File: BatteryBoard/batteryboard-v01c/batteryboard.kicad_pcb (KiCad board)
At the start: 2 copper layers, 95.9 x 90.2 mm, 27 parts, among them J1 KEYSTONE-1042, J12 Screw_Terminal_01x02, J2 KEYSTONE-1042, J3 KEYSTONE-1042, J4 KEYSTONE-1042, J5 KEYSTONE-1042, J6 KEYSTONE-1042, J7 5023520400, J8 Screw_Terminal_01x02, Q1 IRF7458, Q2 IRF7458, U1 R5460N233AF

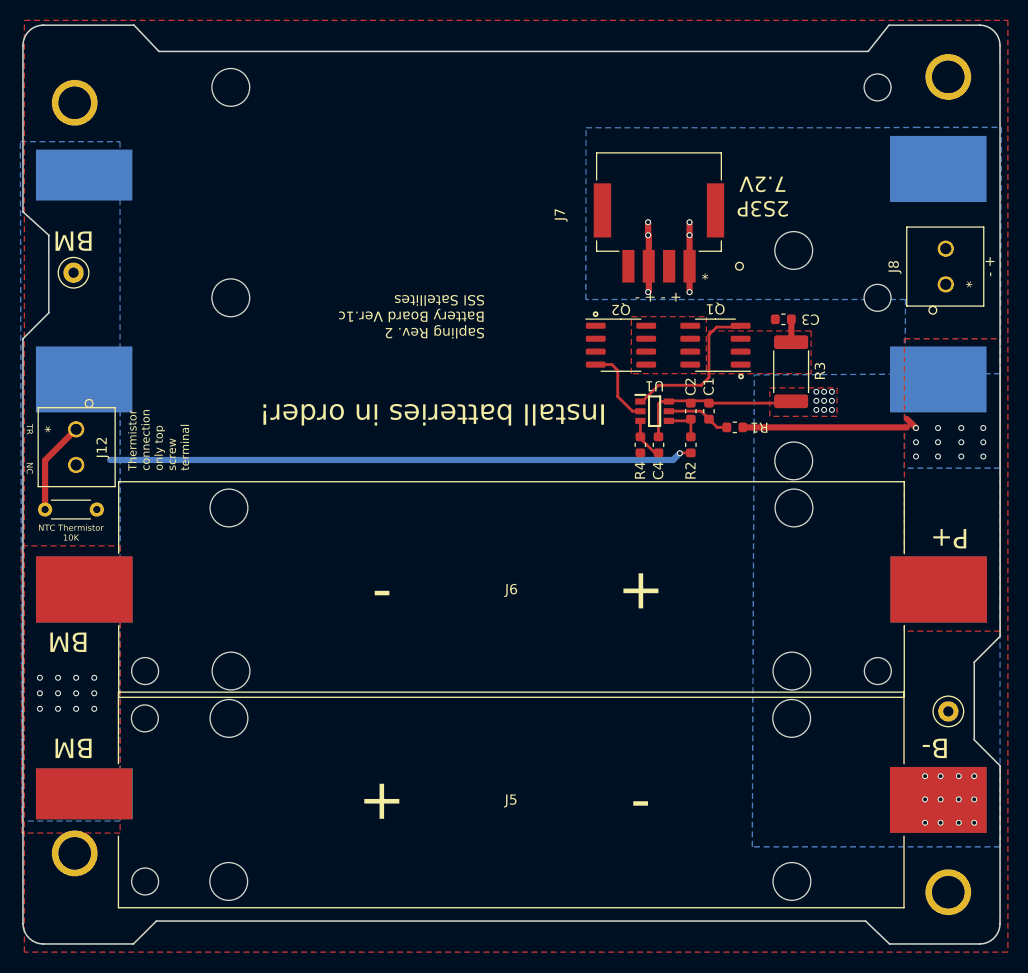
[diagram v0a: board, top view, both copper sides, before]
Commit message: Battery board and side panels ready for CAD check and review, pycubed not finished yet
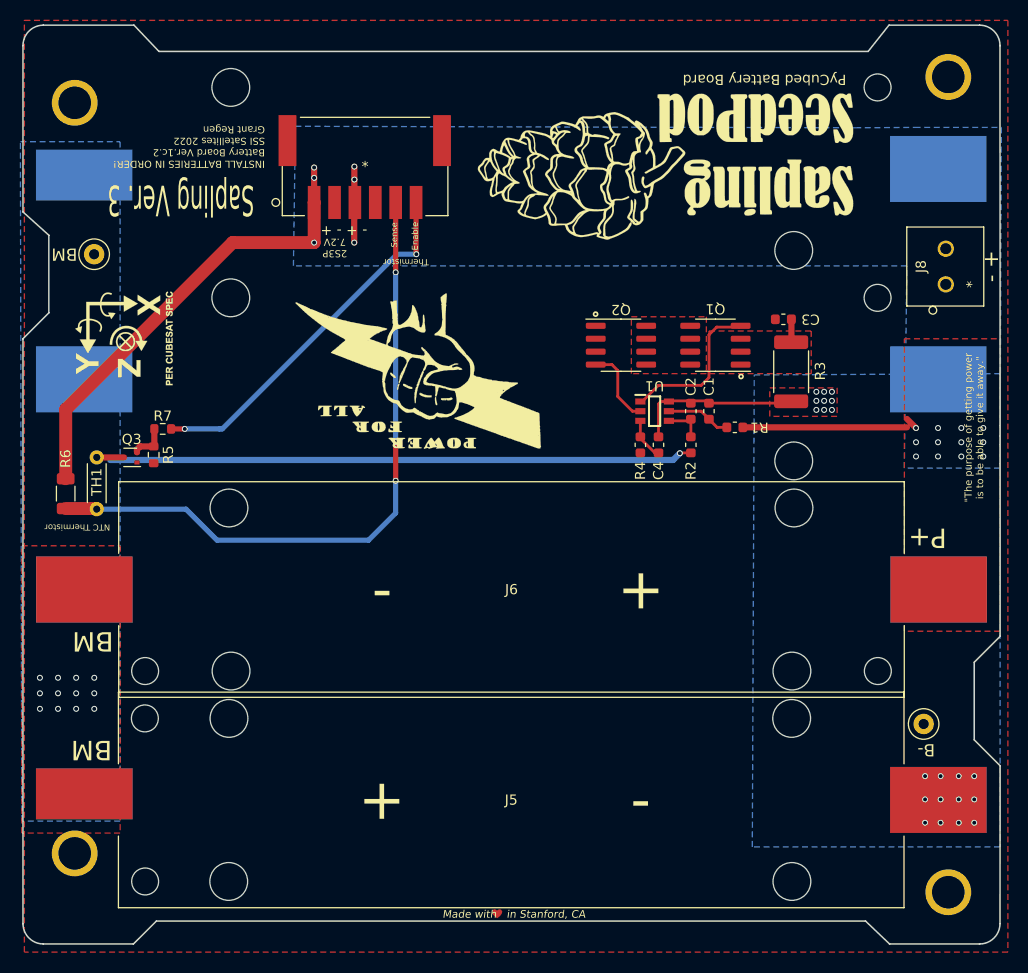
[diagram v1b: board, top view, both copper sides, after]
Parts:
- removed J12: Screw_Terminal_01x02, batteryboard:pheonix_2pos_screwterminal
- added Made with   in Stanford, CA: Val**, batteryboard:SSI_KiCad_Heart, F.Cu at (99.7, 141.1)
- added Q3: MMBT2222AT, Package_TO_SOT_SMD:SOT-523, F.Cu at (63.7, 96.2)
- added R5: 100k, Resistor_SMD:R_0603_1608Metric, F.Cu at (66.0, 96.0)
- added R6: 200k, Resistor_SMD:R_1206_3216Metric, F.Cu at (57.4, 99.8)
- added R7: 200k, Resistor_SMD:R_0603_1608Metric, F.Cu at (66.9, 93.4)
- added Ref**: Val**, batteryboard:XYZ_cubesat-bot, B.Cu at (63.1, 84.5)
- added Ref**: Val**, batteryboard:PowerLogo, F.Cu at (92.4, 87.7)
- added Ref**: Val**, batteryboard:SeedPodLogo, F.Cu at (115.9, 67.0)
- J7: value 5023520400 -> 5023520601; footprint batteryboard:duraclik_4pos -> batteryboard:5023520600
- TH1: value Thermistor -> TTDO-10KC8-3-1%
- moved J7 33.3 mm to (86.8, 67.7)
- moved TH1 5.07 mm to (60.4, 101.3), turned to 90 degrees
- moved TP1 2.72 mm to (141.6, 122.4)
- moved TP2 2.72 mm to (60.2, 76.3)
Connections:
- J7 pad 5: (no net) -> PyCubed_AIN5
- J7 pad 6: (no net) -> DigitalPinTBD
- TH1 pad 1: BAT_THERM -> PyCubed_AIN5
- TH1 pad 2: PACK- -> Net-(Q3-Pad3)
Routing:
- net PyCubed_AIN5: track 0.00 -> 65.3 mm, vias 0 -> 3
- net PACK+: track 31.1 -> 70.2 mm
- net DigitalPinTBD: track 0.00 -> 36.3 mm, vias 0 -> 2
- net BAT_THERM: track 9.14 -> 0.00 mm
- net Net-(Q3-Pad2): track 0.00 -> 3.78 mm
- net Net-(Q3-Pad3): track 0.00 -> 2.66 mm
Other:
- board text added: ""The purpose of getting power is to be able to give it away.""
- board text added: "Enable"
- board text added: "INSTALL BATTERIES IN ORDER! Battery Board Ver.1c.2 SSI Satellites 2022 Grant Regen"
- board text added: "NTC Thermistor"
- board text added: "PyCubed Battery Board"
- board text added: "REGEN"
- board text added: "Sapling Ver. 3"
- board text added: "Sense"
- board text added: "Thermistor"
- board text removed: "Install batteries in order!"
- board text removed: "NC"
- board text removed: "NTC Thermistor 10K"
- board text removed: "Sapling Rev. 2 Battery Board Ver.1c SSI Satellites"
- board text removed: "TR"
- board text removed: "Thermistor connection only top screw terminal"

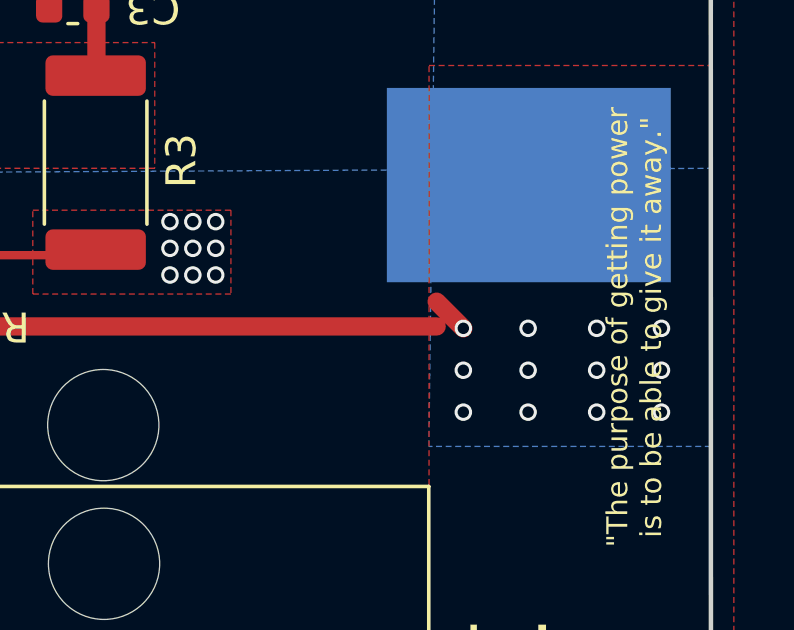
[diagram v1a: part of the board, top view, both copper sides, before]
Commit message: radio and gps moved to make space for limit switches
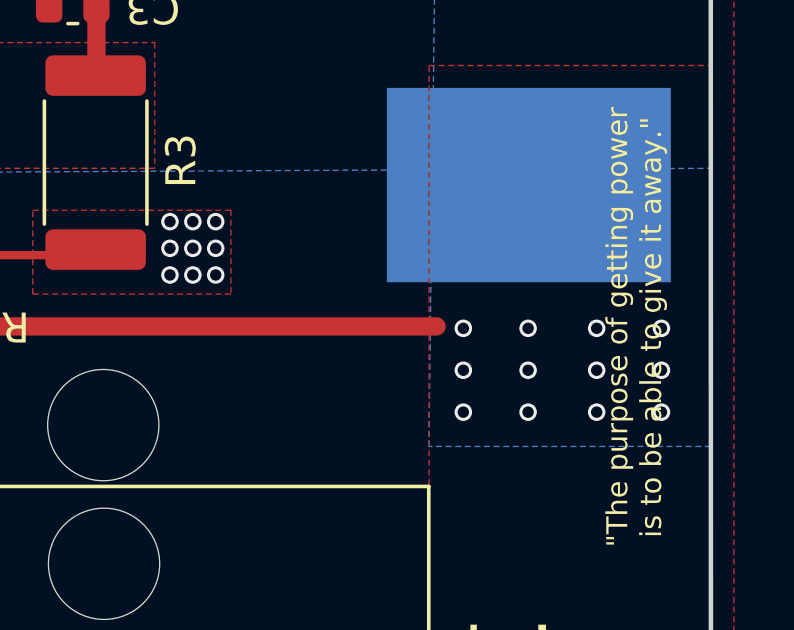
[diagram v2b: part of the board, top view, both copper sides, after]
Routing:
- net PACK+: track 70.2 -> 68.9 mm

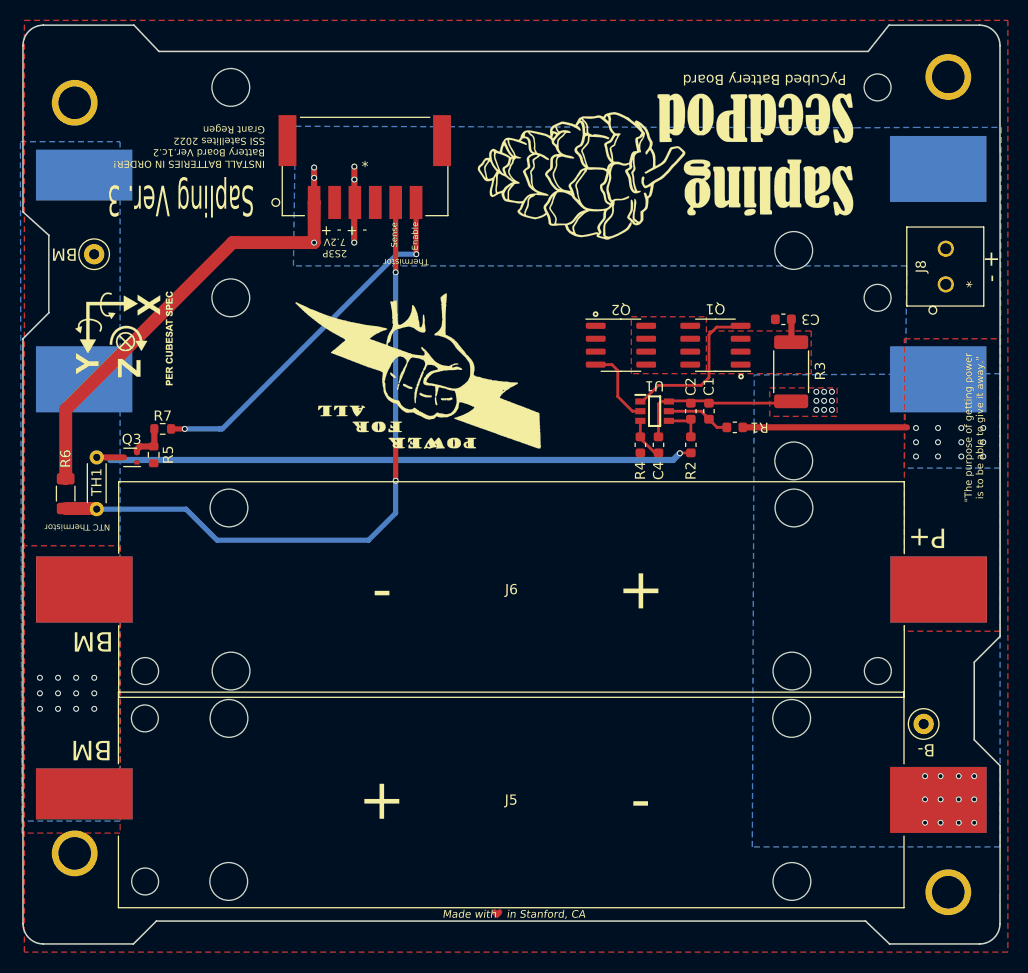
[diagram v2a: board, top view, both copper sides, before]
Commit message: porting over to kicad 6.0, pycubed is functionally done as well as battery
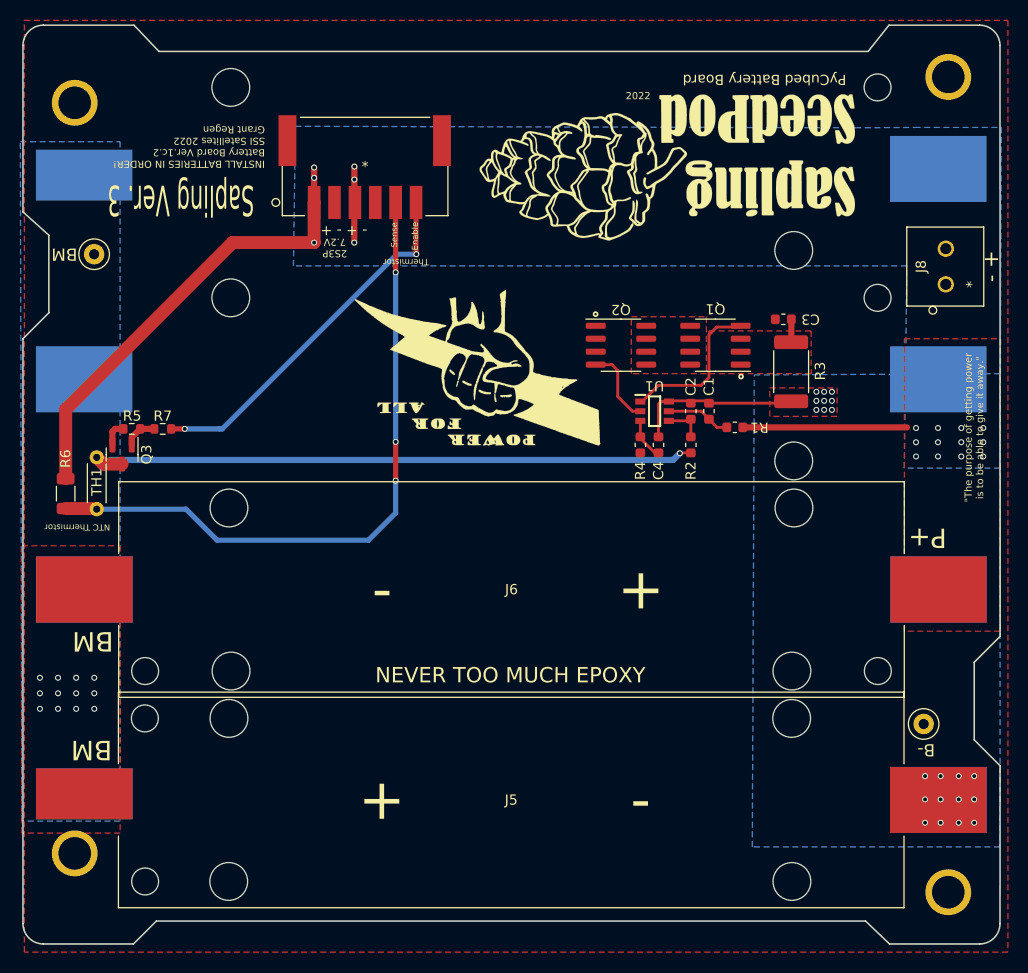
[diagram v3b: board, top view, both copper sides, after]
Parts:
- removed Made with   in Stanford, CA: Val**, batteryboard:SSI_KiCad_Heart
- removed the Ref** at (63.1, 84.5)
- J7: value 5023520601 -> MOLEX 5023520601
- Q3: footprint Package_TO_SOT_SMD:SOT-523 -> Package_TO_SOT_SMD:SOT-23
- moved Ref** 5.83 mm to (98.3, 87.4)
- moved R5 3.33 mm to (63.9, 93.4), turned to 180 degrees
- moved Q3 0.86 mm to (62.9, 95.9), turned to -90 degrees
- moved Ref** 0.19 mm to (116.1, 67.1)
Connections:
- H1 pad 1: (no net) -> unconnected-(H1-Pad1)
- H2 pad 1: (no net) -> unconnected-(H2-Pad1)
- H3 pad 1: (no net) -> unconnected-(H3-Pad1)
- H4 pad 1: (no net) -> unconnected-(H4-Pad1)
- Q3 pad 1: PACK- -> Net-(Q3-Pad1)
- Q3 pad 2: Net-(Q3-Pad2) -> PACK-
- R5 pad 1: Net-(Q3-Pad2) -> Net-(Q3-Pad1)
- R7 pad 1: DigitalPinTBD -> PyCubed_PA20
- R7 pad 2: Net-(Q3-Pad2) -> Net-(Q3-Pad1)
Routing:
- net Net-(Q3-Pad2): track 3.78 -> 0.00 mm
- net Net-(Q3-Pad1): track 0.00 -> 3.31 mm
- net PACK-: track 0.00 -> 2.49 mm
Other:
- net class Default removed
- board text added: "NEVER TOO MUCH EPOXY"
